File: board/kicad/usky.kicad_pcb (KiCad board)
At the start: 2 copper layers, 28 parts, among them J102 USB_A, Q101 NPN, Q102 NPN, Q103 NPN, U101 LM27313-SOT23, U102 STM32F103TB-QFN36, U103 REG113-XX-SOT23, U104 TPD4E1U06-SC70

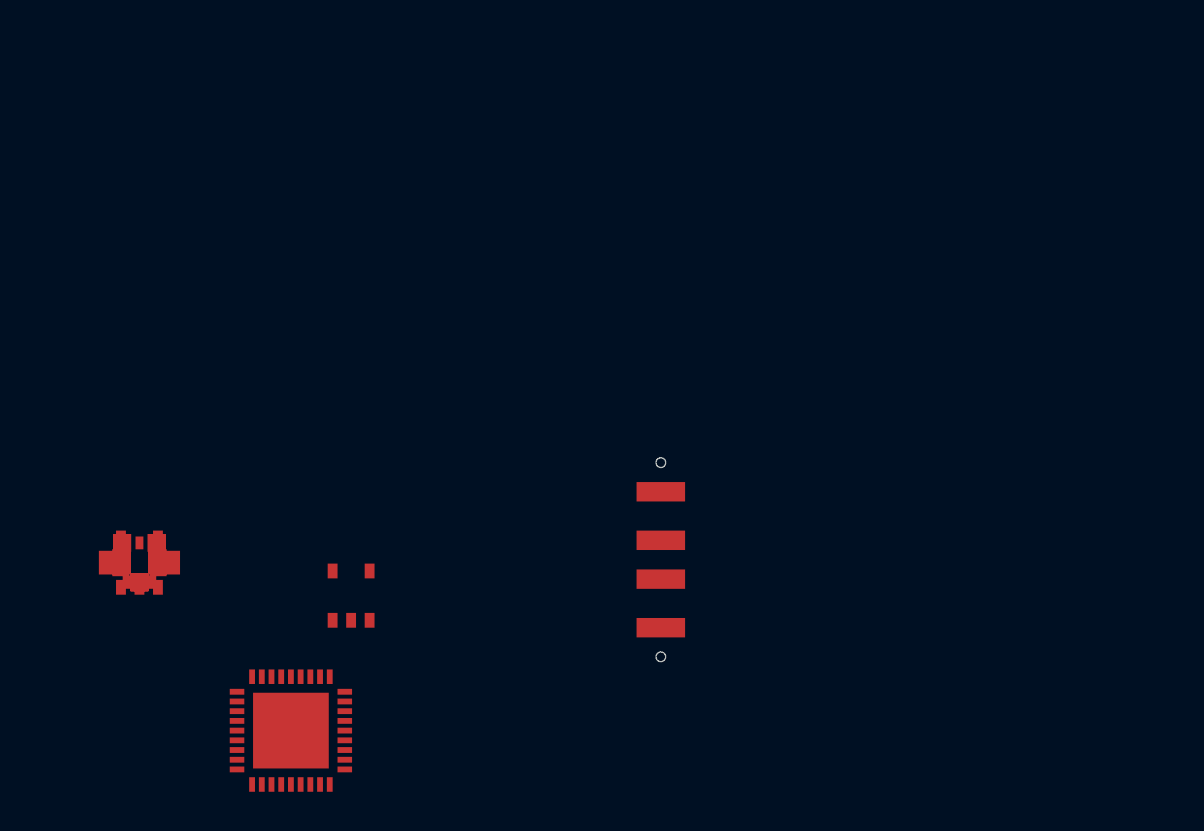
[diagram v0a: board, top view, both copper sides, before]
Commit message: need to change op amp to 2 channel
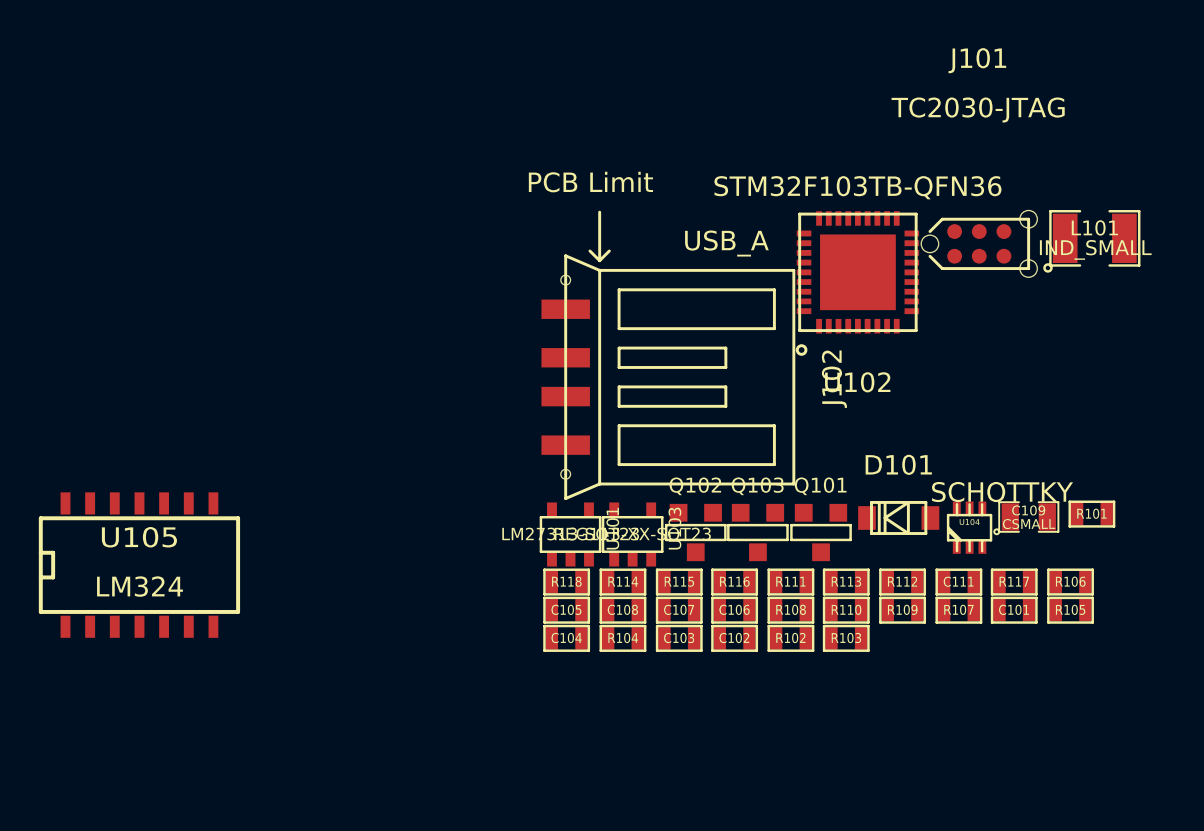
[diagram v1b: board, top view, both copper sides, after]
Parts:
- added C111: CSMALL, SM0603, F.Cu at (42.2, 1.00)
- added J101: TC2030-JTAG, TC2030-NL, F.Cu at (43.2, -17.1)
- added L101: IND_SMALL, SM1210, F.Cu at (49.2, -16.7)
- added R111: RES_0603, SM0603, F.Cu at (33.5, 1.00)
- added R112: RES_0603, SM0603, F.Cu at (39.3, 1.00)
- added R113: RES_0603, SM0603, F.Cu at (36.4, 1.00)
- added R114: RES_0603, SM0603, F.Cu at (24.9, 1.00)
- added R115: 10k, SM0603, F.Cu at (27.8, 1.00)
- added R116: 10k, SM0603, F.Cu at (30.6, 1.00)
- added R117: 10k, SM0603, F.Cu at (45.0, 1.00)
- added R118: 10k, SM0603, F.Cu at (22.0, 1.00)
- added U105: LM324, SO14N, F.Cu at (0.00, 0.00)
- R105, R106: value RES_0603 -> NE
- moved R101 49.1 mm to (49.0, -2.50)
- moved R105 48.0 mm to (48.0, 2.45)
- moved R106 48.0 mm to (48.0, 1.00)
- moved C109 45.9 mm to (45.8, -2.35)
- moved C101 45.1 mm to (45.0, 2.45)
- moved U104 42.8 mm to (42.8, -1.80)
- moved R107 42.3 mm to (42.2, 2.45)
- moved R109 39.4 mm to (39.3, 2.45)
- moved D101 39.2 mm to (39.1, -2.30)
- moved U102 37.5 mm to (37.0, -14.9)
- moved R103 36.6 mm to (36.4, 3.90)
- moved R110 36.5 mm to (36.4, 2.45)
- moved Q101 35.1 mm to (35.1, -1.55)
- moved R102 33.8 mm to (33.5, 3.90)
- moved R108 33.6 mm to (33.5, 2.45)
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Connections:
- C105 pad 1: N-0000040 -> N-0000058
- C105 pad 2: N-0000041 -> N-000006
- Q101 pad 1: N-0000040 -> N-0000015
- Q102 pad 3: N-0000040 -> N-0000058
- R104 pad 1: N-0000040 -> N-0000058
- R105 pad 1: N-0000041 -> N-000006
- R106 pad 2: N-0000041 -> N-000006
- R107 pad 1: /RNG_OUT -> N-0000015

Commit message: first release to be reviewed
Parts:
- removed Q103: NPN, SOT23EBC
- removed R106: NE, SM0603
- removed R114: RES_0603, SM0603
- removed R117, R118: 10k, SM0603
- added C110: 10n, SM0603, F.Cu at (80.0, 41.7)
- added C112: 10p, SM0603, F.Cu at (88.7, 51.3)
- added C113: 100n, SM0603, F.Cu at (75.3, 44.7)
- added C114: 10n, SM0603, F.Cu at (86.0, 50.8)
- added D102: LED, LED-0603, F.Cu at (103.0, 50.5)
- added SW101: SW_PUSH_SMALL, ALPS_SKRKAEE010, F.Cu at (74.6, 50.7)
- added VIA_600_300_GND: VAL**, VIA_600_300_GND, F.Cu at (88.5, 44.0)
- added VIA_600_300_GND: VAL**, VIA_600_300_GND, F.Cu at (74.1, 48.0)
- added VIA_600_300_GND: VAL**, VIA_600_300_GND, F.Cu at (79.1, 44.5)
- added VIA_600_300_GND: VAL**, VIA_600_300_GND, F.Cu at (79.3, 43.5)
- added VIA_600_300_GND: VAL**, VIA_600_300_GND, F.Cu at (79.2, 45.5)
- added VIA_600_300_GND: VAL**, VIA_600_300_GND, F.Cu at (86.4, 48.1)
- added VIA_600_300_GND: VAL**, VIA_600_300_GND, F.Cu at (84.3, 50.7)
- added VIA_600_300_GND: VAL**, VIA_600_300_GND, F.Cu at (104.6, 48.5)
- added VIA_600_300_GND: VAL**, VIA_600_300_GND, F.Cu at (104.2, 51.1)
- added VIA_600_300_GND: VAL**, VIA_600_300_GND, F.Cu at (73.8, 41.8)
- added VIA_600_300_GND: VAL**, VIA_600_300_GND, F.Cu at (94.7, 47.7)
- added VIA_600_300_GND: VAL**, VIA_600_300_GND, F.Cu at (91.0, 50.5)
- added VIA_600_300_GND: VAL**, VIA_600_300_GND, F.Cu at (93.7, 48.7)
- added VIA_600_300_GND: VAL**, VIA_600_300_GND, F.Cu at (95.7, 48.7)
- added VIA_600_300_GND: VAL**, VIA_600_300_GND, F.Cu at (95.7, 46.7)
- added VIA_600_300_GND: VAL**, VIA_600_300_GND, F.Cu at (93.7, 46.7)
- added VIA_600_300_GND: VAL**, VIA_600_300_GND, F.Cu at (94.7, 45.7)
- added VIA_600_300_GND: VAL**, VIA_600_300_GND, F.Cu at (94.7, 49.7)
- added VIA_600_300_GND: VAL**, VIA_600_300_GND, F.Cu at (96.7, 47.7)
- added VIA_600_300_GND: VAL**, VIA_600_300_GND, F.Cu at (92.7, 47.7)
- added VIA_600_300_GND: VAL**, VIA_600_300_GND, F.Cu at (75.0, 49.2)
- added VIA_600_300_GND: VAL**, VIA_600_300_GND, F.Cu at (97.5, 50.8)
- added VIA_600_300_GND: VAL**, VIA_600_300_GND, F.Cu at (103.0, 48.5)
- added VIA_600_300_GND: VAL**, VIA_600_300_GND, F.Cu at (102.7, 43.2)
- added VIA_600_300_GND: VAL**, VIA_600_300_GND, F.Cu at (104.2, 41.1)
- added VIA_600_300_GND: VAL**, VIA_600_300_GND, F.Cu at (83.3, 45.5)
- added VIA_600_300_GND: VAL**, VIA_600_300_GND, F.Cu at (70.8, 51.2)
- added VIA_600_300_GND: VAL**, VIA_600_300_GND, F.Cu at (73.9, 50.7)
- added VIA_600_300_GND: VAL**, VIA_600_300_GND, F.Cu at (75.3, 50.7)
- added VIA_600_300_GND: VAL**, VIA_600_300_GND, F.Cu at (74.9, 47.2)
- added VIA_600_300_GND: VAL**, VIA_600_300_GND, F.Cu at (74.9, 46.1)
- added X101: SMD_XTAL, xtal_3.2x2.5, F.Cu at (88.6, 48.5)
- C111: value CSMALL -> 10p
- R104, R107: value RES_0603 -> 330k
- R105: value NE -> RES_0603
- U105: value LM324 -> TL972; footprint SO14N -> SSOP8
- moved J102 100.2 mm to (107.0, 46.1)
- moved U105 88.5 mm to (74.9, 47.2), turned to 270 degrees
- moved U103 86.2 mm to (100.1, 41.6), turned to 90 degrees
- moved U102 85.2 mm to (94.7, 47.7), turned to 315 degrees
- moved C108 82.4 mm to (96.9, 42.5), turned to 180 degrees
- moved C106 82.0 mm to (102.8, 41.4), turned to 270 degrees
- moved R108 81.1 mm to (99.3, 50.0)
- moved C107 79.1 mm to (96.9, 40.9), turned to 180 degrees
- moved R110 78.9 mm to (100.8, 48.1)
- moved J101 77.8 mm to (92.7, 43.0), turned to 225 degrees
- moved U101 77.0 mm to (83.2, 45.5), turned to 270 degrees
- moved C104 76.6 mm to (82.3, 51.1)
- moved U104 75.9 mm to (101.6, 46.1), turned to 270 degrees
- moved R109 74.3 mm to (100.8, 44.1)
- moved R105 72.0 mm to (101.5, 50.6), turned to 270 degrees
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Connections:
- C102 pad 2: N-0000026 -> /HV
- C103 pad 1: N-0000026 -> /HV
- C104 pad 1: N-0000026 -> /HV
- C105 pad 2: N-000006 -> N-000005
- C111 pad 1: /AV_RNG_OUT -> GND
- C111 pad 2: /RNG_OUT -> N-0000018
- L101 pad 2: N-0000027 -> /sw_1
- R101 pad 1: N-0000045 (its old number) -> /RNG_EN
- R103 pad 2: N-0000026 -> /HV
- R104 pad 2: N-0000026 -> /HV
- R105 pad 1: N-000006 -> N-0000012
- R105 pad 2: N-0000026 -> N-0000013
- R107 pad 2: N-0000026 -> /HV
- R108 pad 1: (no net) -> /USB_PUP
- R111 pad 2: N-000006 -> N-000005
- R115 pad 1: N-0000014 -> N-000006
- R116 pad 2: N-0000014 -> N-000006
- U101 pad 1: N-0000027 -> /sw_1
- U101 pad 4: N-0000045 (its old number) -> /RNG_EN
- U102 pad 12: (no net) -> N-0000013
- U102 pad 15: (no net) -> /USB_PUP
- U102 pad 2: (no net) -> N-0000018
- U102 pad 3: (no net) -> N-000008
- U102 pad 34: (no net) -> /RNG_EN
- U102 pad 37: (no net) -> GND
- U102 pad 8: /RNG_OUT -> /AV_RNG_OUT
- U102 pad 9: (no net) -> N-0000016
- U105 pad 4: +3.3V -> GND
- U105 pad 5: N-0000017 -> N-000006
- U105 pad 6: (no net) -> /Vref
- U105 pad 7: N-0000018 -> /Vref
- U105 pad 8: (no net) -> +3.3V
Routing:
- net +5V: track 0.00 -> 29.4 mm, vias 0 -> 4
- net /AV_RNG_OUT: track 0.00 -> 27.4 mm, vias 0 -> 2
- net N-0000016: track 0.00 -> 18.2 mm, vias 0 -> 2
- net /HV: track 0.00 -> 17.0 mm
- net +3.3V: track 0.00 -> 15.8 mm, vias 0 -> 9
- net /Vref: track 0.00 -> 10.2 mm
- net /RNG_EN: track 0.00 -> 8.98 mm, vias 0 -> 2
- net /DP: track 0.00 -> 8.49 mm, vias 0 -> 2
- net N-0000018: track 0.00 -> 6.66 mm
- net N-0000013: track 0.00 -> 5.96 mm
- net N-000004: track 0.00 -> 5.92 mm
- net /DM: track 0.00 -> 5.68 mm
- net /TDI: track 0.00 -> 5.67 mm, vias 0 -> 2
- net N-0000037: track 0.00 -> 5.53 mm
- net N-0000033: track 0.00 -> 5.36 mm
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- added copper zone on B.Cu, net +3.3V
- added copper zone on F.Cu, net +5V
- added copper zone on F.Cu, net /sw_1
- added copper zone on B.Cu, net GND
- added copper zone on F.Cu, net GND
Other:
- net class 5V added: clearance 0.152, trace_width 0.254, via_dia 0.6, via_drill 0.3
- net class Default: clearance 0.254 -> 0.152; trace_width 0.254 -> 0.152; via_dia 0.889 -> 0.6; via_drill 0.635 -> 0.3
- rule trace_clearance: 0.254 -> 0.152
- rule trace_min: 0.254 -> 0.152
- rule via_min_drill: 0.508 -> 0.3
- rule via_min_size: 0.889 -> 0.6

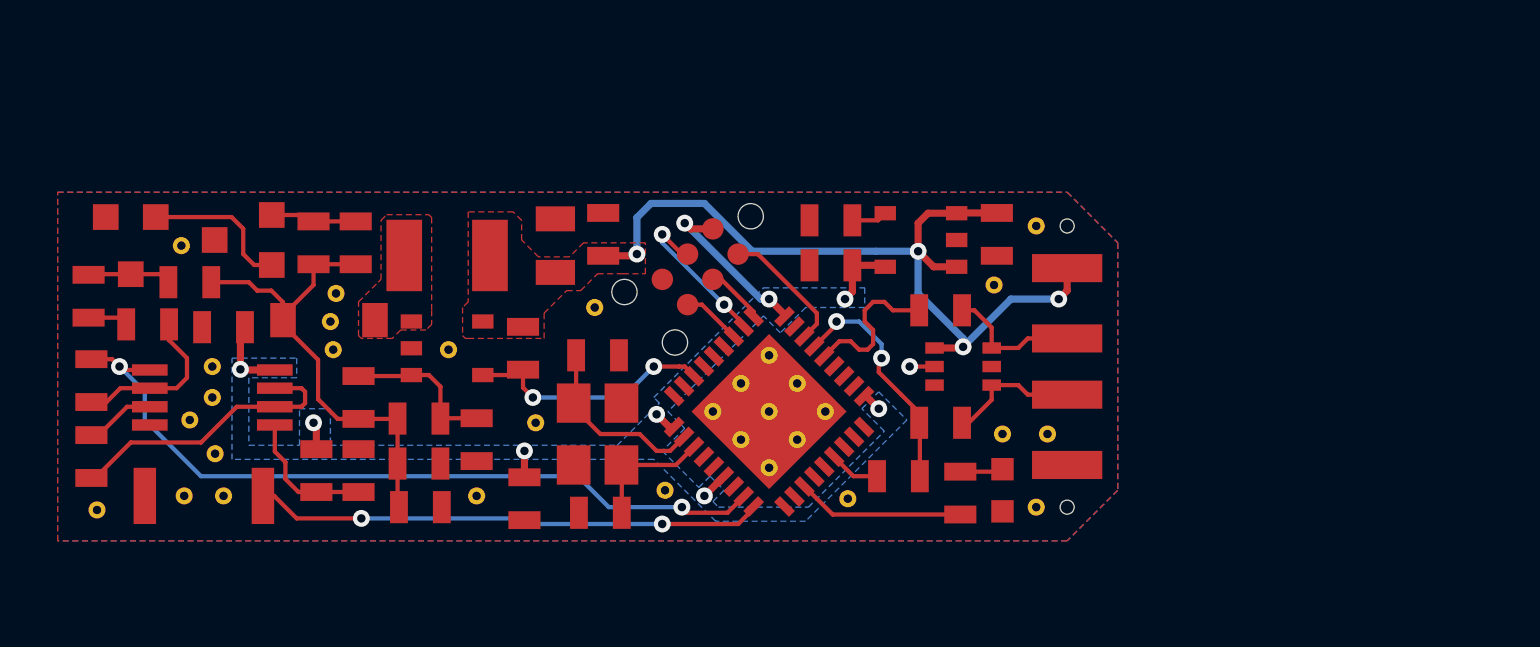
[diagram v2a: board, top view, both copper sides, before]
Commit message: changed usky project to Kicad post revolution format
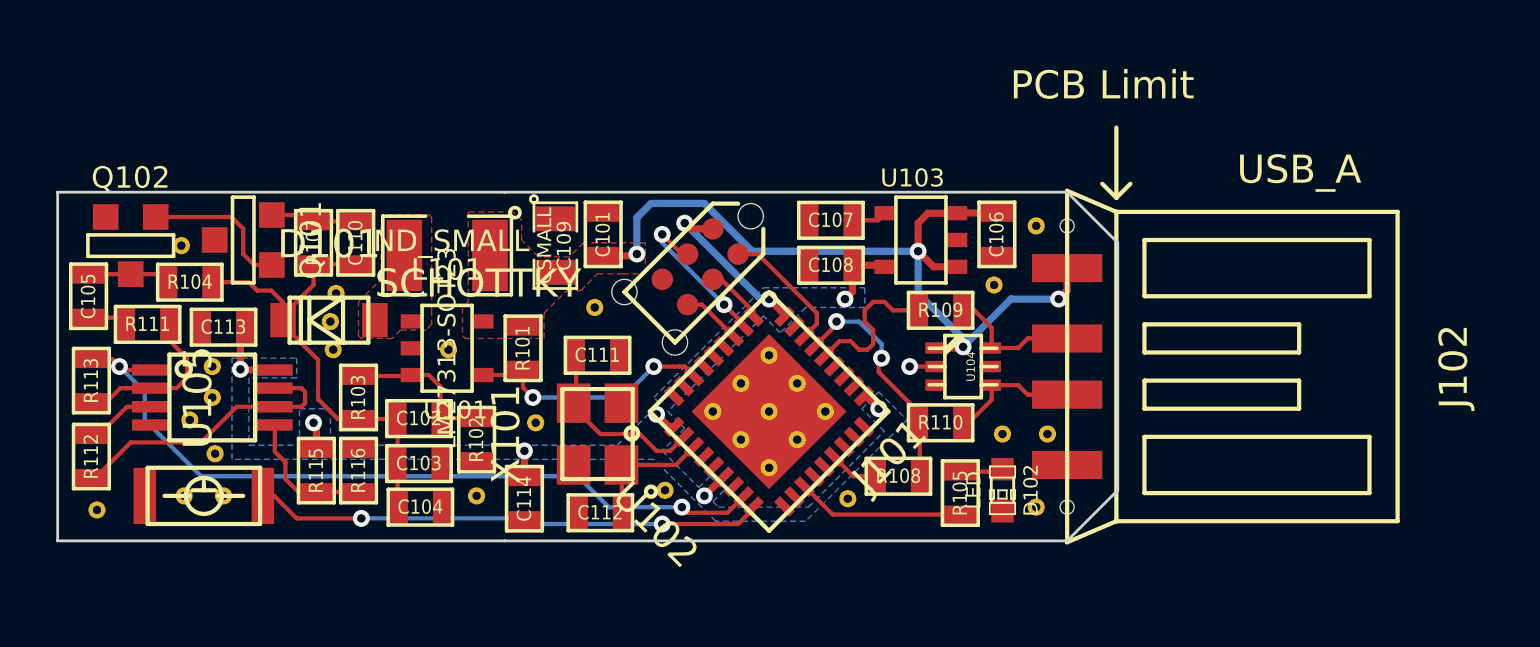
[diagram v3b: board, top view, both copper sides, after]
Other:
- board outline added: 37.7 x 12.4 mm

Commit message: broken ! transistor lib change
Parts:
- added VIA_600_300_GND: VAL**, VIA_Workaround:VIA_600_300_GND, F.Cu at (95.2, 41.0)
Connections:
- Q101 pad 3: (no net) -> Net-(Q101-Pad3)
- U102 pad 10: (no net) -> Net-(U102-Pad10)
- U102 pad 11: (no net) -> Net-(U102-Pad11)
- U102 pad 13: (no net) -> Net-(U102-Pad13)
- U102 pad 14: (no net) -> Net-(U102-Pad14)
- U102 pad 16: (no net) -> Net-(U102-Pad16)
- U102 pad 17: (no net) -> Net-(U102-Pad17)
- U102 pad 20: (no net) -> Net-(U102-Pad20)
- U102 pad 21: (no net) -> Net-(U102-Pad21)
- U102 pad 22: (no net) -> Net-(U102-Pad22)
- U102 pad 31: (no net) -> Net-(U102-Pad31)
- U102 pad 32: (no net) -> Net-(U102-Pad32)
- U102 pad 33: (no net) -> Net-(U102-Pad33)
- U102 pad 35: (no net) -> Net-(U102-Pad35)
- U102 pad 4: (no net) -> Net-(U102-Pad4)
- U102 pad 7: (no net) -> Net-(U102-Pad7)
- U104 pad 3: (no net) -> Net-(U104-Pad3)
- U104 pad 5: (no net) -> Net-(U104-Pad5)

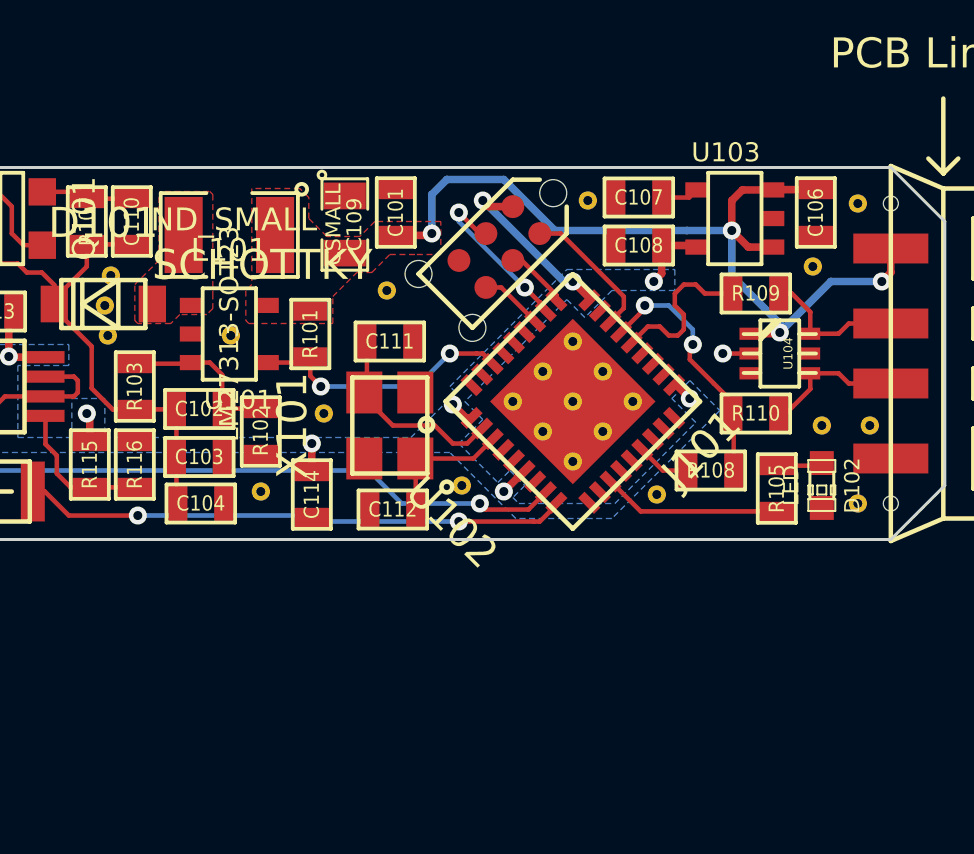
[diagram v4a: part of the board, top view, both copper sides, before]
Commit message: changed qfn36 footprint, need to fix the pcb
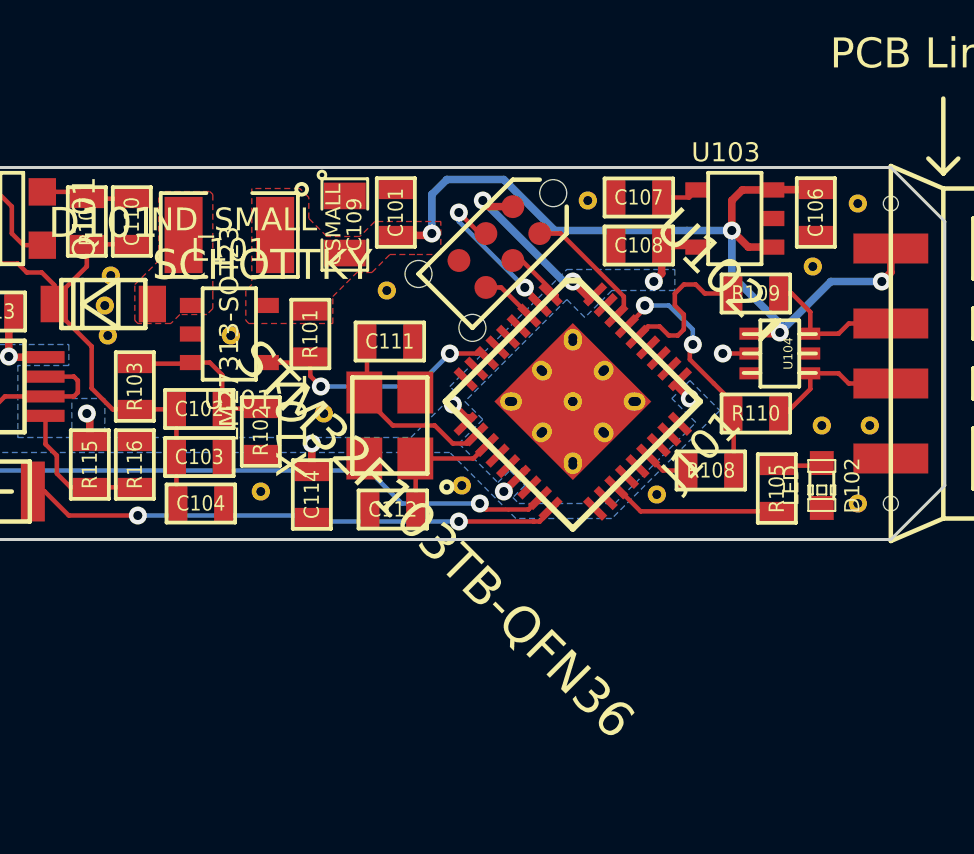
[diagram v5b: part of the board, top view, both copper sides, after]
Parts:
- U102: footprint QFN36_6x6_0.5mm -> QFN:QFN36_6x6_0.5mm
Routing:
- net GND: track 0.88 -> 16.4 mm, vias 1 -> 3
- net Net-(SW101-Pad2): track 18.2 -> 3.83 mm, vias 2 -> 1
- net /TDI: track 5.67 -> 1.19 mm, vias 2 -> 1
- net Net-(U102-Pad32): track 0.00 -> 4.32 mm
- net /DM: track 5.68 -> 1.36 mm
- net /TMS: track 4.69 -> 0.70 mm
- net +3.3V: track 15.8 -> 12.3 mm, vias 9 -> 5
- net /RNG_EN: track 8.98 -> 12.3 mm
- net Net-(C111-Pad2): track 6.66 -> 9.96 mm, vias 0 -> 1
- net /AV_RNG_OUT: track 27.4 -> 24.9 mm
- net Net-(U102-Pad17): track 0.00 -> 2.52 mm
- net Net-(U102-Pad33): track 0.00 -> 2.02 mm, vias 0 -> 1
- net /TDO: track 2.11 -> 0.51 mm
- net Net-(U102-Pad21): track 0.00 -> 1.42 mm
- net Net-(U102-Pad11): track 0.00 -> 1.18 mm
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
